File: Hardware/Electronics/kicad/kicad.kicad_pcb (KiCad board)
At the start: 2 copper layers, 28 x 130 mm, 47 parts, among them J1 Conn_01x03_Socket, J2 Conn_01x03_Socket, J3 Conn_01x03_Socket, J6 USB_C_Receptacle_USB2.0_16P, SW1 SW_Push, SW2 SW_Push, SW3 SW_Push, U1 USBLC6-2P6, U2 MCP73831-2-OT, U3 ESP32-C3-MINI-1-N4, U4 XC6210B332MR, U5 TPS61023DRLR, U6 SN74LV1T34DBV

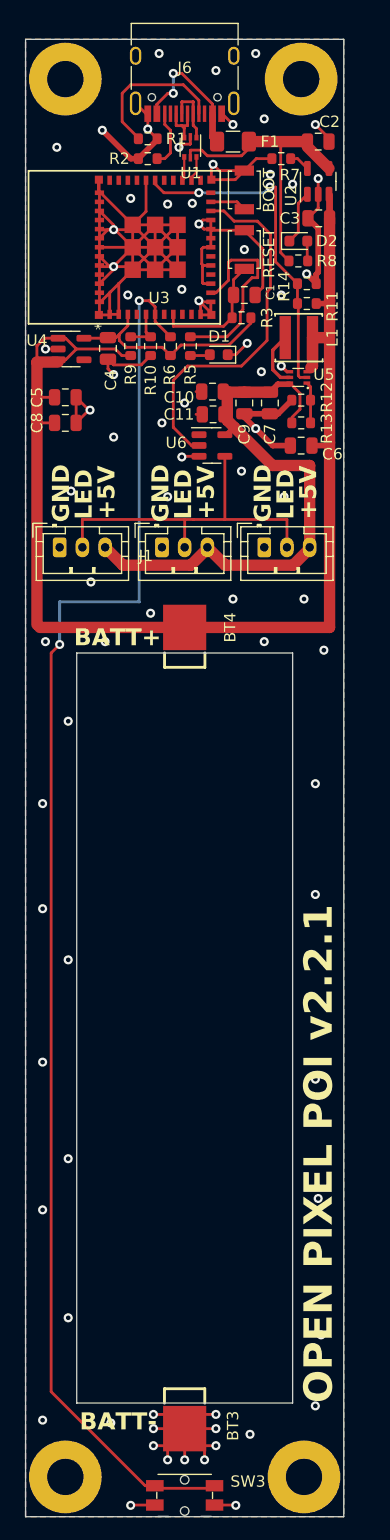
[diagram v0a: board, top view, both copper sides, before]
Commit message: Add Clock pinout & FPC connectors to PCB, start on basic ws2812b LED strip.
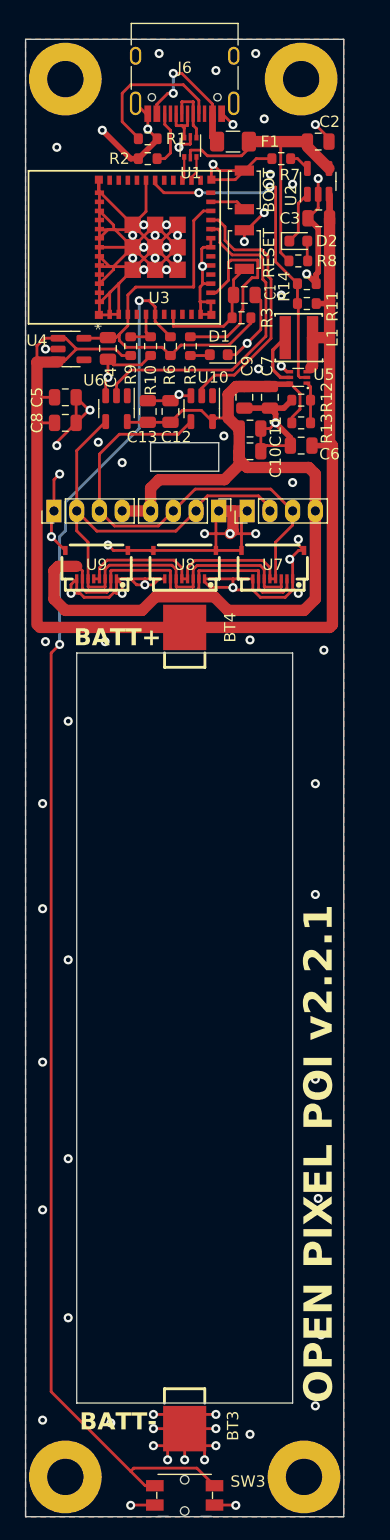
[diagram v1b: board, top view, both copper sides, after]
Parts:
- removed J1, J2, J3: Conn_01x03_Socket, Connector_JST:JST_PH_B3B-PH-K_1x03_P2.00mm_Vertical
- added C12: 1u, Capacitor_SMD:C_0805_2012Metric, F.Cu at (62.8, 62.8)
- added C13: 100n, Capacitor_SMD:C_0805_2012Metric, F.Cu at (60.8, 62.8)
- added J4: Conn_01x04, Connector_PinHeader_2.00mm:PinHeader_1x04_P2.00mm_Vertical, F.Cu at (52.5, 71.5)
- added J5: Conn_01x04, Connector_PinHeader_2.00mm:PinHeader_1x04_P2.00mm_Vertical, F.Cu at (69.5, 71.5)
- added J7: Conn_01x04, Connector_PinHeader_2.00mm:PinHeader_1x04_P2.00mm_Vertical, F.Cu at (67.0, 71.5)
- added U10: SN74LV1T34DBV, Package_TO_SOT_SMD:SOT-23-5, F.Cu at (65.5, 62.5)
- added U7: FPC-0.5HF-8PWBH10, easyeda2kicad:FPC-SMD_8P-P0.50_XUNPU_FPC-0.5HF-8PWBH10, F.Cu at (71.8, 76.2)
- added U8: FPC-0.5HF-8PWBH10, easyeda2kicad:FPC-SMD_8P-P0.50_XUNPU_FPC-0.5HF-8PWBH10, F.Cu at (64.0, 76.2)
- added U9: FPC-0.5HF-8PWBH10, easyeda2kicad:FPC-SMD_8P-P0.50_XUNPU_FPC-0.5HF-8PWBH10, F.Cu at (56.2, 76.2)
- moved U6 9.00 mm to (58.0, 62.5), turned to -90 degrees
- moved C10 6.20 mm to (69.8, 66.2), turned to 180 degrees
- moved C11 3.48 mm to (69.8, 64.2), turned to 180 degrees
- moved C7 0.50 mm to (71.5, 61.5)
- moved C9 0.50 mm to (69.2, 61.5)
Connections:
- U3 pad 20: -BATT -> LED Data
- U3 pad 21: -BATT -> LED Clock
- U3 pad 22: LED Data -> +3.3V
- U6 pad 4: Net-(J1-Pin_2) -> LED Data 5V
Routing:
- net -BATT: track 222.9 -> 303.0 mm, vias 77 -> 89
- net +5V: track 49.9 -> 115.7 mm
- net LED Clock 5V: track 0.00 -> 61.5 mm
- net LED Data 5V: track 0.00 -> 60.4 mm
- net Net-(J1-Pin_2): track 30.9 -> 0.00 mm
- net LED Clock: track 0.00 -> 23.0 mm
- net +3.3V: track 19.6 -> 35.1 mm
- net LED Data: track 32.3 -> 29.3 mm
- net POI SW: track 126.1 -> 125.3 mm
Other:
- outline, holes or cut-outs redrawn
- board text added: "<MIRROR>"
- board text added: "CLOCK"
- board text added: "DATA"
- board text removed: "LED"

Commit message: Add 20 and 55 pixel strips
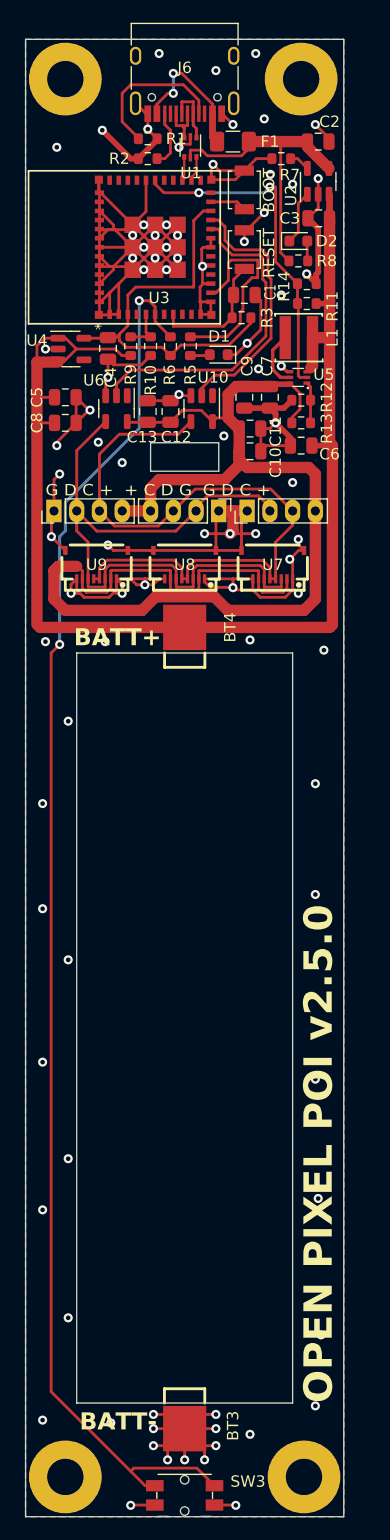
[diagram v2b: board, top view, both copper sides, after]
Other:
- board text added: "G D C + + C D G G D C +"
- board text added: "I created this project to provide a cheap yet capable poi option to the community. It has a simple set of functionality to keep the focus on use and spinning. It is fully open souce and intended to be DIY, to encourage making, and full ownership of our technology. More Info is available at github.com/mitchlol/Open-Pixel-Poi including all the source code and documentation. Mitch."
- board text added: "OPEN PIXEL POI v2.5.0"
- board text removed: "I created this project to provide a cheap yet capable poi option to the community. It has a simple set of functionality to keep the focus on use and spinning. It is fully open souce and intended to be DIY, to encourage making, and full ownership of our technology. Suggested donation of 5$ per set of poi built via paypal. Link is available at github.com/mitchlol/Open-Pixel-Poi along with all the s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"
- board text removed: "OPEN PIXEL POI v2.2.1"

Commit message: Add pullup to gpio8, change board "version" to 3.0.0 due to new data pinout.
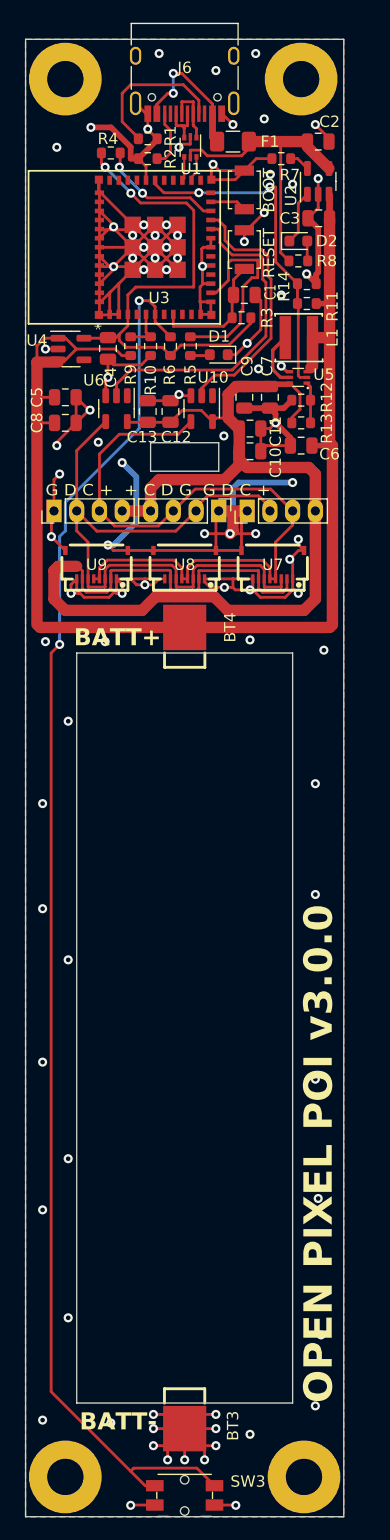
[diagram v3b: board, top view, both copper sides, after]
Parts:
- added R4: 10k, Resistor_SMD:R_0603_1608Metric, F.Cu at (57.5, 40.0)
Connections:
- U3 pad 22: +3.3V -> GPIO8
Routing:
- net -BATT: track 303.0 -> 321.1 mm, vias 89 -> 92
- net GPIO8: track 0.00 -> 11.1 mm, vias 0 -> 2
- net +3.3V: track 35.1 -> 45.0 mm, vias 0 -> 2
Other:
- board text added: "OPEN PIXEL POI v3.0.0"
- board text removed: "OPEN PIXEL POI v2.5.0"
